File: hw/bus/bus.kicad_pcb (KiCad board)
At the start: 2 copper layers, 99.1 x 99.1 mm, 1218 parts, among them J10 IDE STM bus, J11 IDE STM bus, J12 IDE STM bus, J13 IDE STM bus, J14 IDE STM bus, J15 IDE STM bus, J16 IDE STM bus, J17 IDE STM bus, J18 IDE STM bus, J19 IDE STM bus, J3 IDE STM bus, J4 IDE STM bus, J5 IDE STM bus, J6 IDE STM bus, J7 IDE STM bus, J8 IDE STM bus, J9 IDE STM bus

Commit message: added capacitor at volatage regulator input
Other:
- board text added: "https://github.com/johannesloetzsch/pillbus v0.1.0"
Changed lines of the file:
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@@
+		)
+	)
+	(gr_text "https://github.com/johannesloetzsch/pillbus v0.1.0"
+		(at 147.828 149.6314 0)
+		(layer "F.SilkS")
+		(effects
+			(font
+				(size 0.8 0.8)
+				(thickness 0.1)
+			)
+			(justify right bottom)
 		)
 	)

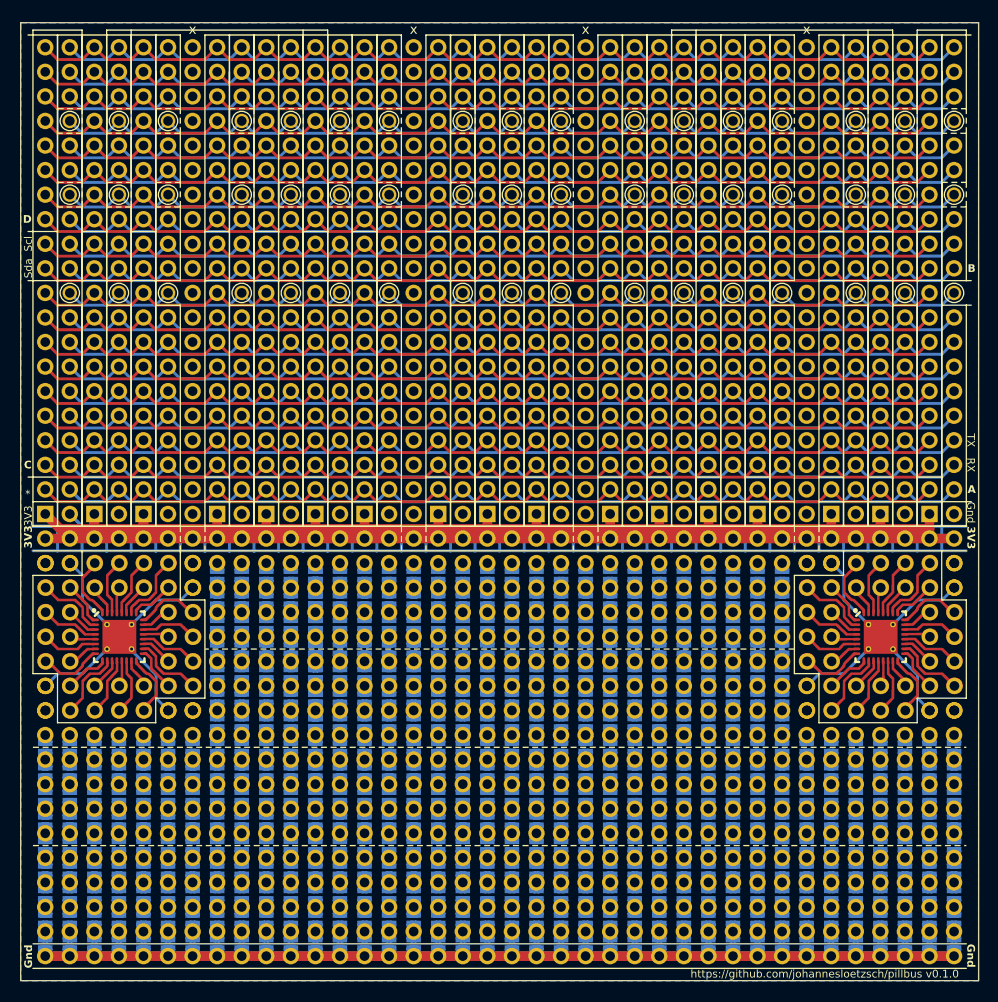
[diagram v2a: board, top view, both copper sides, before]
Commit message: changed layout of bus board
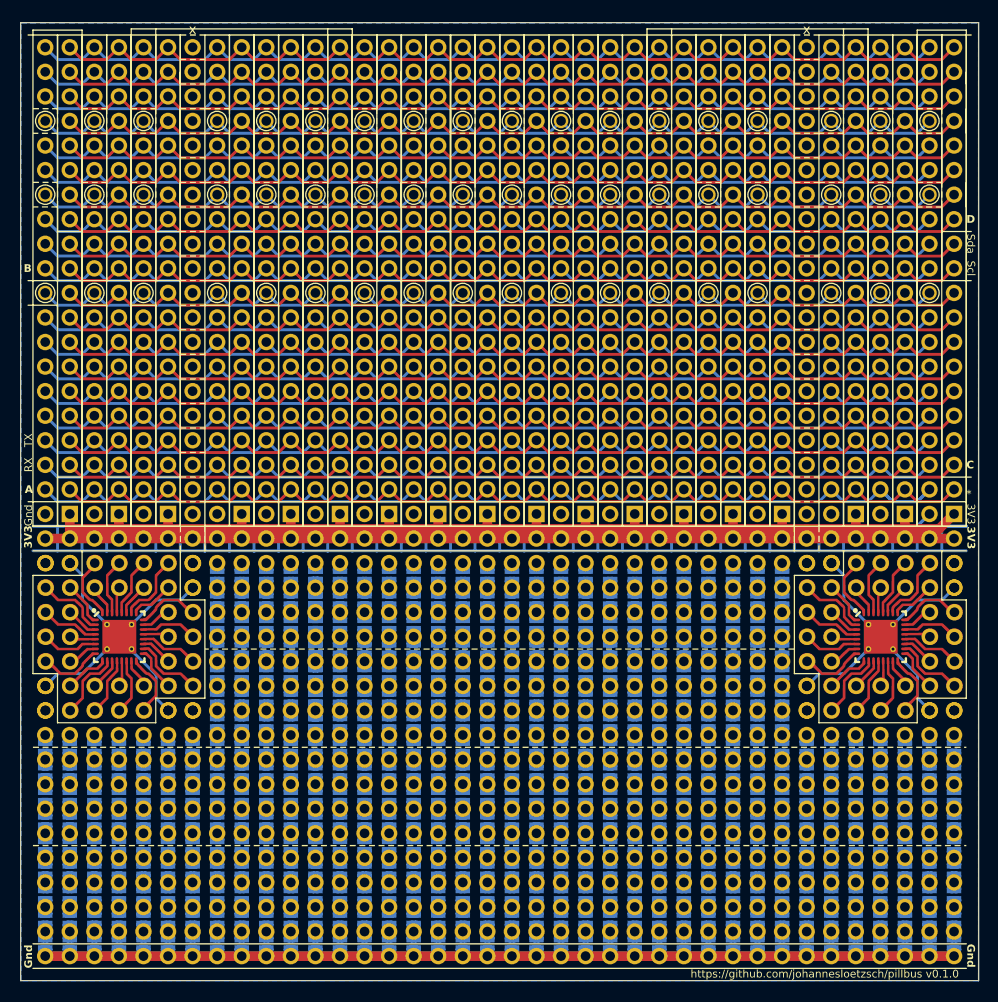
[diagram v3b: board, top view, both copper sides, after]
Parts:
- removed J10, J18, J19, J8, J9: IDE STM bus, ribbon:IDE STM bus
- removed the REF** at (68.6, 88.9)
- removed the REF** at (68.6, 81.3)
- removed the REF** at (91.4, 55.9)
- removed the REF** at (132.1, 99.1)
- removed the REF** at (132.1, 71.1)
- removed the REF** at (109.2, 66.0)
- removed the REF** at (91.4, 63.5)
- removed the REF** at (132.1, 76.2)
- removed the REF** at (68.6, 83.8)
- removed the REF** at (91.4, 91.4)
- removed the REF** at (132.1, 58.4)
- removed the REF** at (68.6, 58.4)
- removed the REF** at (132.1, 68.6)
- removed the REF** at (109.2, 88.9)
- removed the REF** at (68.6, 68.6)
- removed the REF** at (91.4, 78.7)
- removed the REF** at (109.2, 71.1)
- removed the REF** at (91.4, 81.3)
- removed the REF** at (68.6, 73.7)
- removed the REF** at (68.6, 55.9)
- removed the REF** at (68.6, 76.2)
- removed the REF** at (91.4, 86.4)
- removed the REF** at (68.6, 101.6)
- removed the REF** at (68.6, 94.0)
- removed the REF** at (91.4, 83.8)
- removed the REF** at (109.2, 81.3)
- removed the REF** at (68.6, 63.5)
- removed the REF** at (109.2, 86.4)
- removed the REF** at (68.6, 53.3)
- removed the REF** at (109.2, 101.6)
- removed the REF** at (109.2, 99.1)
- removed the REF** at (91.4, 76.2)
- removed the REF** at (132.1, 83.8)
- removed the REF** at (68.6, 71.1)
- removed the REF** at (109.2, 78.7)
- removed the REF** at (109.2, 94.0)
- removed the REF** at (132.1, 94.0)
- removed the REF** at (68.6, 78.7)
- removed the REF** at (91.4, 71.1)
- removed the REF** at (91.4, 58.4)
- removed the REF** at (109.2, 96.5)
- removed the REF** at (91.4, 73.7)
- removed the REF** at (109.2, 68.6)
- removed the REF** at (132.1, 63.5)
- removed the REF** at (109.2, 83.8)
- removed the REF** at (68.6, 61.0)
- removed the REF** at (109.2, 53.3)
- removed the REF** at (132.1, 66.0)
- removed the REF** at (109.2, 73.7)
- removed the REF** at (132.1, 96.5)
- removed the REF** at (132.1, 81.3)
- removed the REF** at (109.2, 55.9)
- removed the REF** at (68.6, 99.1)
- removed the REF** at (109.2, 63.5)
- removed the REF** at (91.4, 61.0)
- removed the REF** at (132.1, 78.7)
- removed the REF** at (132.1, 53.3)
- removed the REF** at (91.4, 94.0)
- removed the REF** at (91.4, 88.9)
- removed the REF** at (132.1, 86.4)
- removed the REF** at (68.6, 66.0)
- removed the REF** at (109.2, 58.4)
- removed the REF** at (109.2, 61.0)
- removed the REF** at (132.1, 61.0)
- removed the REF** at (91.4, 68.6)
- removed the REF** at (68.6, 91.4)
- removed the REF** at (132.1, 91.4)
- removed the REF** at (91.4, 96.5)
- removed the REF** at (109.2, 76.2)
- removed the REF** at (91.4, 99.1)
- removed the REF** at (91.4, 53.3)
- removed the REF** at (109.2, 91.4)
- removed the REF** at (132.1, 73.7)
- removed the REF** at (132.1, 101.6)
- removed the REF** at (91.4, 66.0)
- removed the REF** at (132.1, 55.9)
- removed the REF** at (132.1, 88.9)
- removed the REF** at (91.4, 101.6)
- removed the REF** at (68.6, 96.5)
- removed the REF** at (68.6, 86.4)
- removed Vcc1, Vcc10, Vcc11, Vcc12, Vcc13, Vcc14, Vcc15, Vcc16, Vcc17, Vcc18, Vcc19, Vcc2, Vcc20, Vcc21, Vcc22, Vcc23, Vcc24, Vcc25, Vcc26, Vcc27, Vcc28, Vcc29, Vcc3, Vcc30, Vcc31, Vcc32, Vcc33, Vcc34, Vcc35, Vcc36, Vcc37, Vcc38, Vcc4, Vcc5, Vcc6, Vcc7, Vcc8, Vcc9: ~, base:PTH 1.7mm
- added ?: , , F.Cu at (61.0, 104.1)
- added ?: , , F.Cu at (132.1, 91.4)
- added ?: , , F.Cu at (68.6, 99.1)
- added ?: , , F.Cu at (68.6, 73.7)
- added ?: , , F.Cu at (68.6, 81.3)
- added ?: , , F.Cu at (132.1, 96.5)
- added ?: , , F.Cu at (127.0, 104.1)
- added ?: , , F.Cu at (68.6, 55.9)
- added ?: , , F.Cu at (68.6, 63.5)
- added ?: , , F.Cu at (132.1, 58.4)
- added ?: , , F.Cu at (132.1, 104.1)
- added ?: , , F.Cu at (76.2, 104.1)
- added ?: , , F.Cu at (78.7, 104.1)
- added ?: , , F.Cu at (63.5, 104.1)
- added ?: , , F.Cu at (53.3, 104.1)
- added ?: , , F.Cu at (94.0, 104.1)
- added ?: , , F.Cu at (83.8, 104.1)
- added ?: , , F.Cu at (71.1, 104.1)
- added ?: , , F.Cu at (132.1, 68.6)
- added ?: , , F.Cu at (68.6, 68.6)
- added ?: , , F.Cu at (58.4, 104.1)
- added ?: , , F.Cu at (66.0, 104.1)
- added ?: , , F.Cu at (99.1, 104.1)
- added ?: , , F.Cu at (132.1, 101.6)
- added ?: , , F.Cu at (132.1, 83.8)
- added ?: , , F.Cu at (86.4, 104.1)
- added ?: , , F.Cu at (134.6, 104.1)
- added ?: , , F.Cu at (132.1, 88.9)
- added ?: , , F.Cu at (88.9, 104.1)
- added ?: , , F.Cu at (132.1, 63.5)
- added ?: , , F.Cu at (55.9, 104.1)
- added ?: , , F.Cu at (68.6, 91.4)
- added ?: , , F.Cu at (106.7, 104.1)
- added ?: , , F.Cu at (132.1, 86.4)
- added ?: , , F.Cu at (132.1, 53.3)
- added ?: , , F.Cu at (137.2, 104.1)
- added ?: , , F.Cu at (132.1, 99.1)
- added ?: , , F.Cu at (68.6, 61.0)
- added ?: , , F.Cu at (104.1, 104.1)
- added ?: , , F.Cu at (68.6, 53.3)
- added ?: , , F.Cu at (81.3, 104.1)
- added ?: , , F.Cu at (68.6, 83.8)
- added ?: , , F.Cu at (68.6, 71.1)
- added ?: , , F.Cu at (129.5, 104.1)
- added ?: , , F.Cu at (132.1, 71.1)
- added ?: , , F.Cu at (68.6, 101.6)
- added ?: , , F.Cu at (132.1, 55.9)
- added ?: , , F.Cu at (142.2, 104.1)
- added ?: , , F.Cu at (132.1, 76.2)
- added ?: , , F.Cu at (144.8, 104.1)
- added ?: , , F.Cu at (132.1, 73.7)
- added ?: , , F.Cu at (68.6, 78.7)
- added ?: , , F.Cu at (132.1, 61.0)
- added ?: , , F.Cu at (132.1, 94.0)
- added ?: , , F.Cu at (132.1, 66.0)
- added ?: , , F.Cu at (91.4, 104.1)
- added ?: , , F.Cu at (147.3, 104.1)
- added ?: , , F.Cu at (68.6, 86.4)
- added ?: , , F.Cu at (121.9, 104.1)
- added ?: , , F.Cu at (132.1, 78.7)
- added ?: , , F.Cu at (116.8, 104.1)
- added ?: , , F.Cu at (114.3, 104.1)
- added ?: , , F.Cu at (68.6, 88.9)
- added ?: , , F.Cu at (124.5, 104.1)
- added ?: , , F.Cu at (111.8, 104.1)
- added ?: , , F.Cu at (139.7, 104.1)
- added ?: , , F.Cu at (119.4, 104.1)
- added ?: , , F.Cu at (68.6, 66.0)
- added ?: , , F.Cu at (68.6, 58.4)
- added ?: , , F.Cu at (132.1, 81.3)
- added ?: , , F.Cu at (96.5, 104.1)
- added ?: , , F.Cu at (109.2, 104.1)
- added ?: , , F.Cu at (68.6, 96.5)
- added ?: , , F.Cu at (73.7, 104.1)
- added ?: , , F.Cu at (68.6, 76.2)
- added ?: , , F.Cu at (101.6, 104.1)
- added ?: , , F.Cu at (68.6, 94.0)
- added ?: , , F.Cu at (68.6, 104.1)
- added J1: IDE STM bus, ribbon:IDE STM bus, F.Cu at (147.3, 101.6)
- added J11: IDE STM bus, ribbon:IDE STM bus, F.Cu at (88.9, 101.6)
- added J11: IDE STM bus, ribbon:IDE STM bus, F.Cu at (94.0, 101.6)
- added J11: IDE STM bus, ribbon:IDE STM bus, F.Cu at (109.2, 101.6)
- added J11: IDE STM bus, ribbon:IDE STM bus, F.Cu at (104.1, 101.6)
- added J2: IDE STM bus, ribbon:IDE STM bus, F.Cu at (142.2, 101.6)
- moved J12 10.2 mm to (83.8, 101.6)
- moved J5 10.2 mm to (124.5, 101.6)
- moved J16 10.2 mm to (61.0, 101.6)
- moved J15 10.2 mm to (66.0, 101.6)
- moved J4 10.2 mm to (129.5, 101.6)
- moved J13 7.62 mm to (78.7, 101.6)
- moved J14 7.62 mm to (73.7, 101.6)
- moved J3 7.62 mm to (137.2, 101.6)
- moved J6 7.62 mm to (119.4, 101.6)
- moved J7 7.62 mm to (114.3, 101.6)
- moved J17 7.62 mm to (55.9, 101.6)
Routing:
- net +3.3V: track 228.8 -> 226.3 mm
- net /x20: track 108.3 -> 109.3 mm
- net /B1: track 108.3 -> 109.3 mm
- net /B7: track 108.3 -> 109.3 mm
- net /A7: track 108.3 -> 109.3 mm
- net /A1: track 108.3 -> 109.3 mm
- net /A0: track 114.4 -> 115.5 mm
- net /A4: track 108.3 -> 109.3 mm
- net /C2: track 108.3 -> 109.3 mm
- net /C1: track 108.3 -> 109.3 mm
- net /C0: track 108.3 -> 109.3 mm
- net /B6: track 108.3 -> 109.3 mm
- net /B3: track 108.3 -> 109.3 mm
- net /B0: track 108.3 -> 109.3 mm
- net /A5: track 108.3 -> 109.3 mm
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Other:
- board text added: "${REFERENCE}"
